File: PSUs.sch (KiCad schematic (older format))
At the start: 37 parts, among them U1 LM2674N-ADJ, U11 MCP4151-103E/P, U12 MCP4151-103E/P, U2 LM2574N-3.3, U3 LM2674N-ADJ

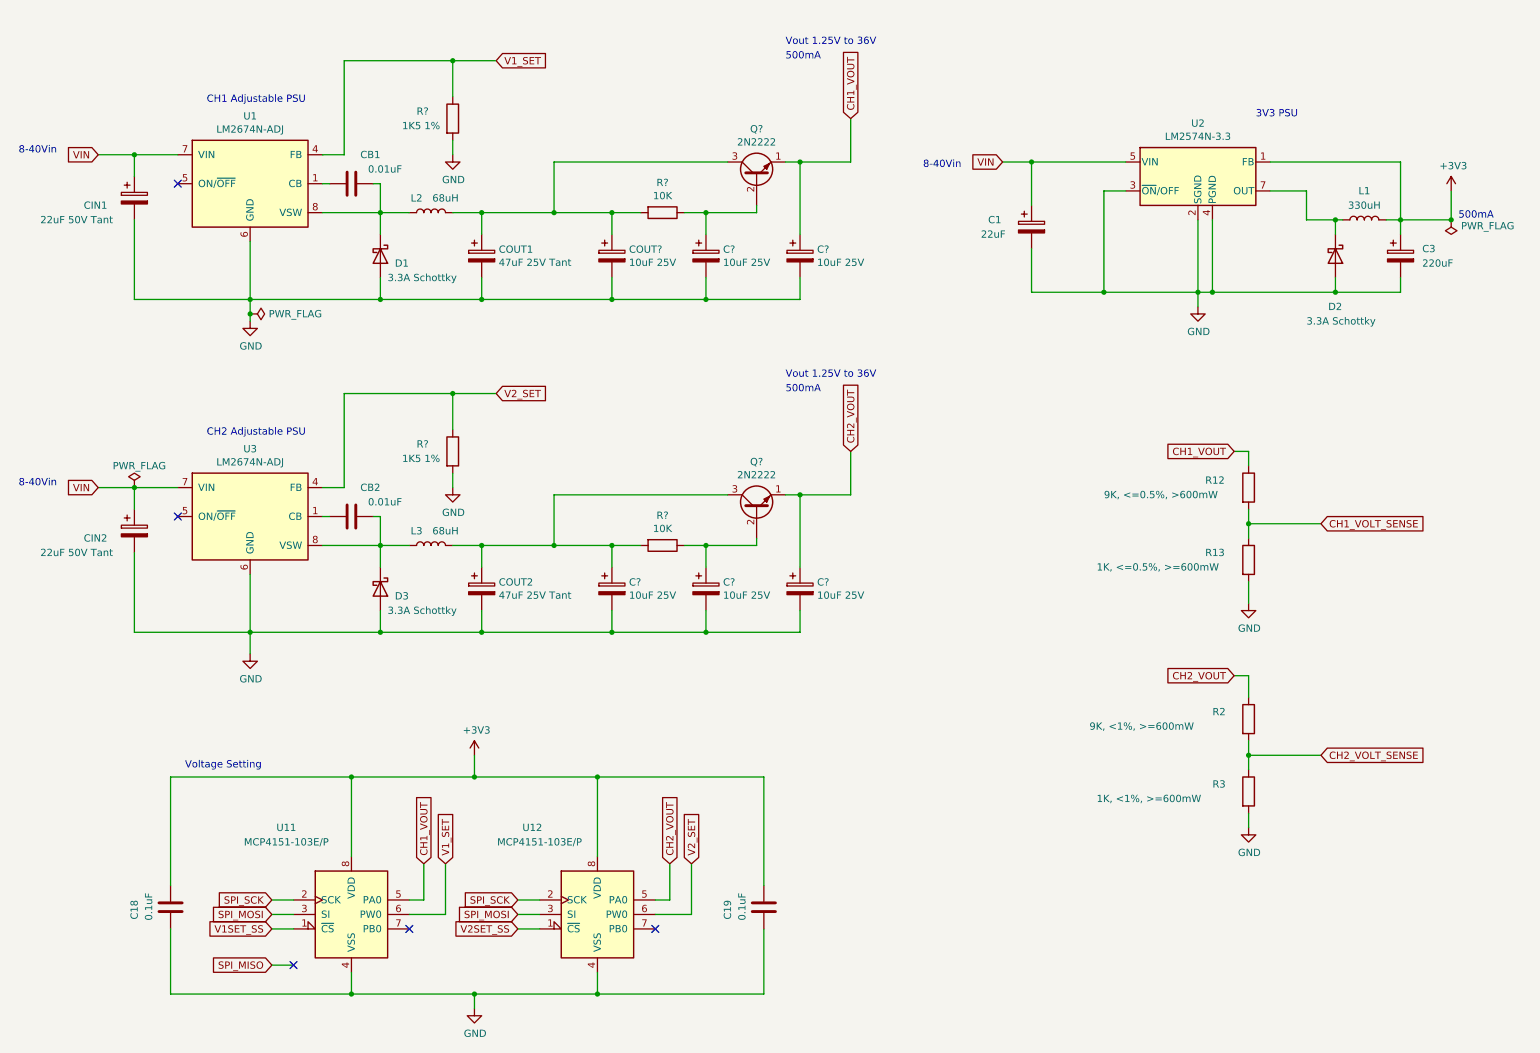
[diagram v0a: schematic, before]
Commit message: Replaced digital pots with analog, removed spi bus too as no longer needed
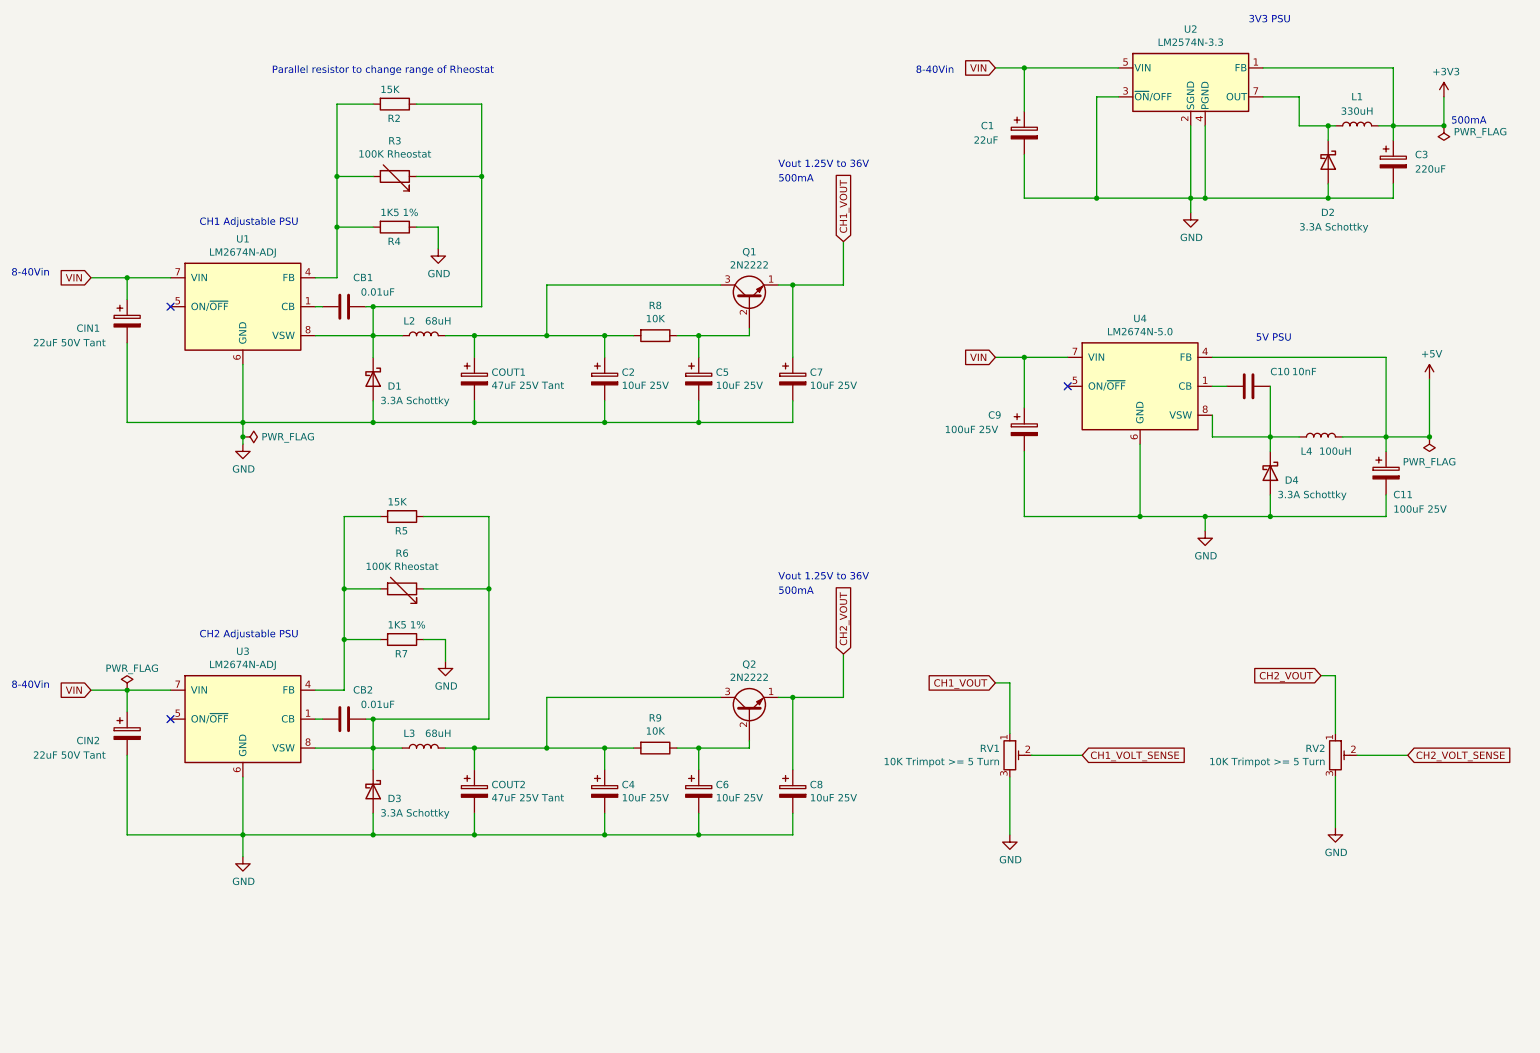
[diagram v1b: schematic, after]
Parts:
- removed C18, C19: 0.1uF, symbol Device:C
- removed R12: 9K, <=0.5%, >600mW, symbol Device:R
- removed R13: 1K, <=0.5%, >=600mW, symbol Device:R
- removed R3: 1K, <1%, >=600mW, symbol Device:R
- removed R?: 1K5 1%, symbol Device:R
- removed U11, U12: MCP4151-103E/P, symbol Potentiometer_Digital:MCP41010
- added C10: 10nF, symbol Device:C
- added C11, C9: 100uF 25V, symbol Device:CP
- added D4: 3.3A Schottky, symbol Device:D_Schottky
- added L4: 100uH, symbol Device:L
- added R3, R6: 100K Rheostat, symbol Device:R_Variable
- added R5: 15K, symbol Device:R
- added R7: 1K5 1%, symbol Device:R
- added RV1, RV2: 10K Trimpot >= 5 Turn, symbol Device:R_POT_TRIM
- added U4: LM2674N-5.0, Package_DIP:DIP-8_W7.62mm, symbol Regulator_Switching:LM2674N-5.0
- R2: value 9K, <1%, >=600mW -> 15K
- gave numbers to parts that had none: 11
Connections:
- net CH1_VOLT_SENSE: now also RV1.2
- net CH1_VOUT: now also RV1.1
- net CH2_VOLT_SENSE: now also RV2.2; no longer R2.2
- net CH2_VOUT: now also RV2.1; no longer R2.1
- net GND: now also R4.1, C11.2, C9.2, D4.2 (A), R7.1, RV1.3, RV2.3, U4.6 (GND); no longer R4.2
- net VIN: now also C9.1, U4.7 (VIN)
- net at CB2.2, D3.1 (K), L3.1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: now also R5.1, R6.1
- net at CB1.2, D1.1 (K), L2.1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: now also R2.1, R3.1
- net V1_SET: no longer names the net of U1.4 (FB)
- net V1_SET: now also R2.2, R4.2, R3.2; no longer R4.1
- net V2_SET: no longer names the net of U3.4 (FB)
- net V2_SET: now also R5.2, R6.2, R7.2
- new net: C10.2, U4.1 (CB)
- new net: C10.1, D4.1 (K), L4.1, U4.8 (VSW)
- new net +5V: C11.1, L4.2, U4.4 (FB)
- no-connect marks 5 -> 3
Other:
- note added: "5V PSU"
- note added: "Parallel resistor to change range of Rheostat"
- note removed: "Voltage Setting"
- moved on the sheet: C1, C2, C3, C4, C5, C6, C7, C8, CB1, CB2, CIN1, CIN2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

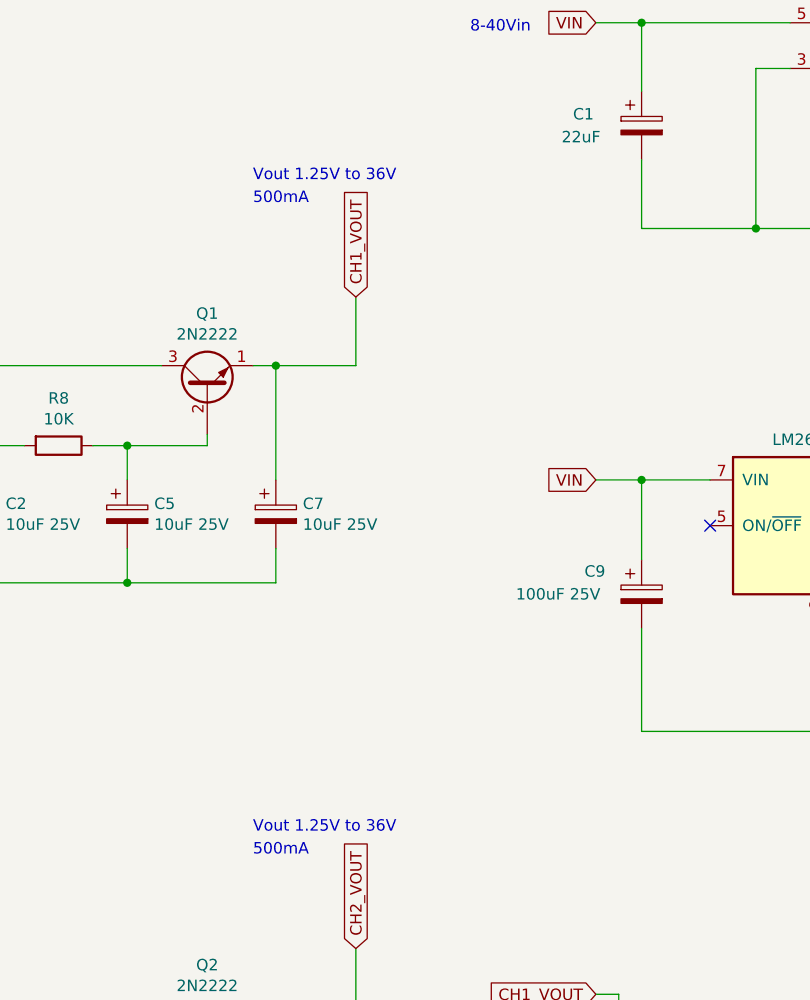
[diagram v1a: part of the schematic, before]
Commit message: corrected some psu errors
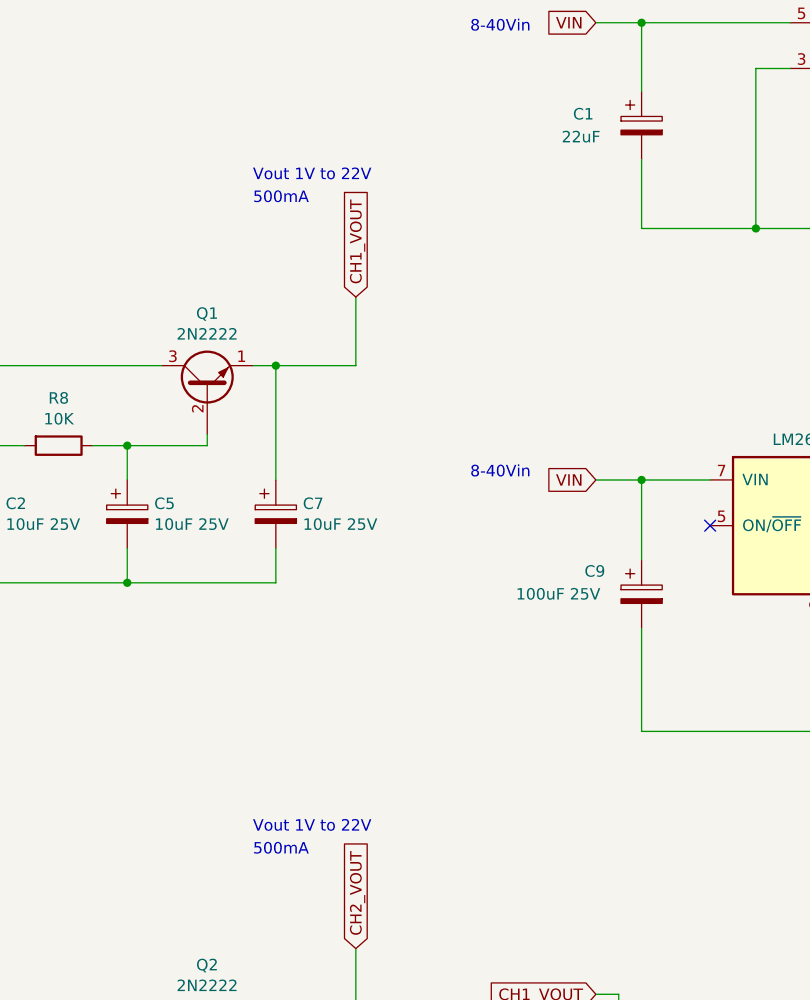
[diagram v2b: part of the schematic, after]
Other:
- note added: "Vout 1V to 22V\n"
- note removed: "Vout 1.25V to 36V\n"
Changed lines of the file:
@@
 	3200 5450 3200 5650
 Text Notes 6000 4500 0    50   ~ 0
-Vout 1.25V to 36V\n
+Vout 1V to 22V\n
 Text Notes 6000 4600 0    50   ~ 0
 500mA\n
@@
 500mA\n
 Text Notes 6000 1650 0    50   ~ 0
-Vout 1.25V to 36V\n
+Vout 1V to 22V\n
 Wire Wire Line
 	3200 2600 3200 2800
@@
 Text Notes 9300 2850 0    50   ~ 0
 5V PSU
+Text Notes 6950 2950 0    50   ~ 0
+8-40Vin
 $EndSCHEMATC
